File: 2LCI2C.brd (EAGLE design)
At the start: 40 x 20 mm, 38 parts, among them IC1 HX711-SOP16L, IC2 HX711-SOP16L, IC3 ATTINY84-SOIC14, J1 ICSP-PIN, J3 Load Cell, J4 Load Cell, Q1 2N3906, Q2 2N3906

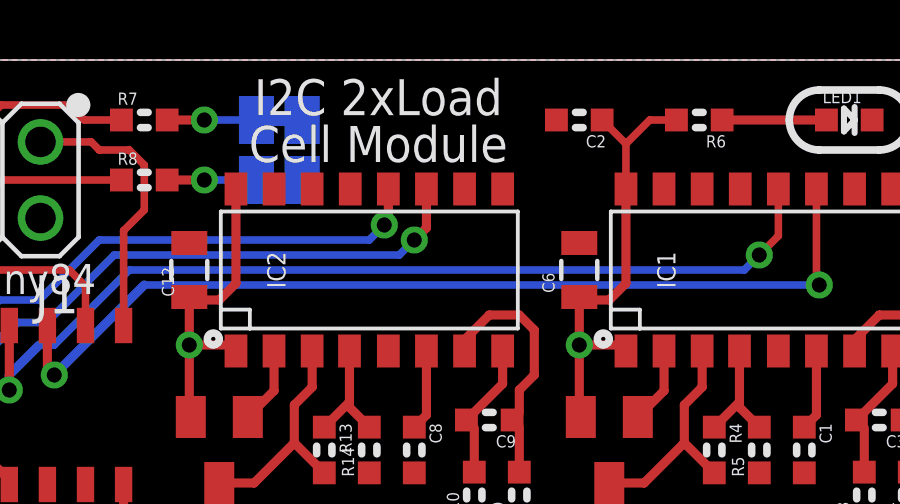
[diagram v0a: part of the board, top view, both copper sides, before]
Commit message: Changed sample rate from 10Hz to 80Hz
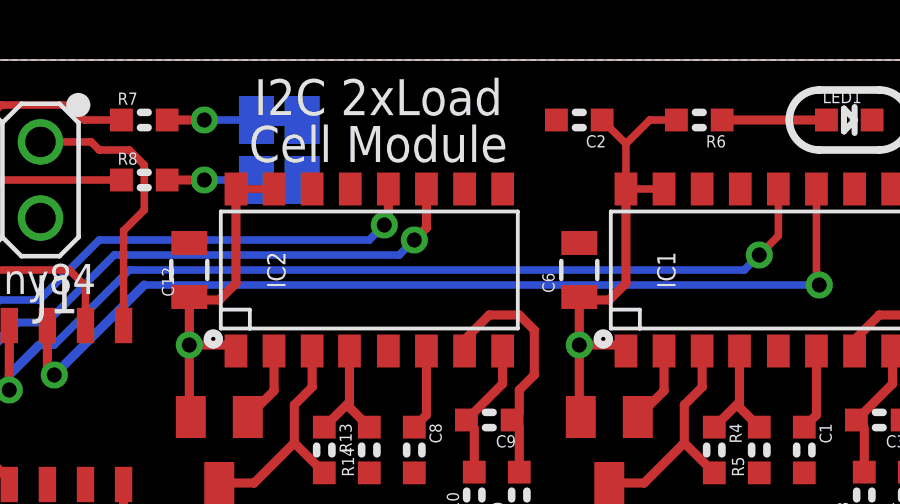
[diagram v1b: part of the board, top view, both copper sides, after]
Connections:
- net GND: no longer IC1.15, IC2.15
- net VCC: now also IC1.15, IC2.15
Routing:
- net VCC: track 34.5 -> 37.0 mm
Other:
- board text added: "v1.0"
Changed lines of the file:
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@@
 </layers>
 <board>
-<fusionsync huburn="a.cGVyc29uYWw6dWUyZDliZmNi" projecturn="a.cGVyc29uYWw6dWUyZDliZmNiIzIwMjAwNjA1MzA0OTA2NTgx" f3durn="urn:adsk.wipprod:dm.lineage:xVkUg9DcS7uGuJ_e9RHQ6Q" pcbguid="" lastpulledtime="" lastsyncedchangeguid="658b777b-6f72-af3e-08d3-df1b217e5c50" latestrevisionid="7995fdce-4818-4739-b131-21203edd6466" lastsyncedrevisionid="7995fdce-4818-4739-b131-21203edd6466" lastboardhashguid="d6e5dbb6-b330-d021-be14-3f51137d8661" lastpushedtime="2020-06-30T10:32:49Z" linktopcb3d="true"/>
+<fusionsync huburn="a.cGVyc29uYWw6dWUyZDliZmNi" projecturn="a.cGVyc29uYWw6dWUyZDliZmNiIzIwMjAwNjA1MzA0OTA2NTgx" f3durn="urn:adsk.wipprod:dm.lineage:xVkUg9DcS7uGuJ_e9RHQ6Q" pcbguid="" lastpulledtime="" lastsyncedchangeguid="658b777b-6f72-af3e-08d3-df1b217e5c50" latestrevisionid="7995fdce-4818-4739-b131-21203edd6466" lastsyncedrevisionid="7995fdce-4818-4739-b131-21203edd6466" lastboardhashguid="d6e5dbb6-b330-d021-be14-3f51137d8661" lastpushedtime="2020-06-30T10:32:49Z" linktopcb3d="false"/>
 <plain>
 <wire x1="0" y1="18" x2="0" y2="2" width="0" layer="20"/>
@@
 <wire x1="19.5" y1="16" x2="19.5" y2="18" width="0.254" layer="22"/>
 <wire x1="18.5" y1="19" x2="19.5" y2="18" width="0.254" layer="22" curve="-90"/>
+<text x="10.42" y="10.3" size="1" layer="22" font="vector" ratio="18" distance="30" rot="MR0">v1.0</text>
 </plain>
 <attributes>
@@
 <contactref element="C8" pad="2"/>
 <contactref element="IC2" pad="14"/>
-<contactref element="IC2" pad="15"/>
 <contactref element="R14" pad="1"/>
 <contactref element="C10" pad="2"/>
@@
 <contactref element="C1" pad="2"/>
 <contactref element="IC1" pad="14"/>
-<contactref element="IC1" pad="15"/>
 <contactref element="C6" pad="2"/>
 <contactref element="J1" pad="6"/>
@@
 <wire x1="4.19" y1="5.85" x2="2.55" y2="5.85" width="0.3048" layer="1"/>
 <wire x1="2.55" y1="5.85" x2="2" y2="5.9" width="0.254" layer="1"/>
+<contactref element="IC1" pad="15"/>
+<contactref element="IC2" pad="15"/>
+<wire x1="16.825" y1="15.7" x2="15.555" y2="15.7" width="0.254" layer="1"/>
+<wire x1="29.825" y1="15.7" x2="28.555" y2="15.7" width="0.254" layer="1"/>
 </signal>
 <signal name="SCK_SCL">

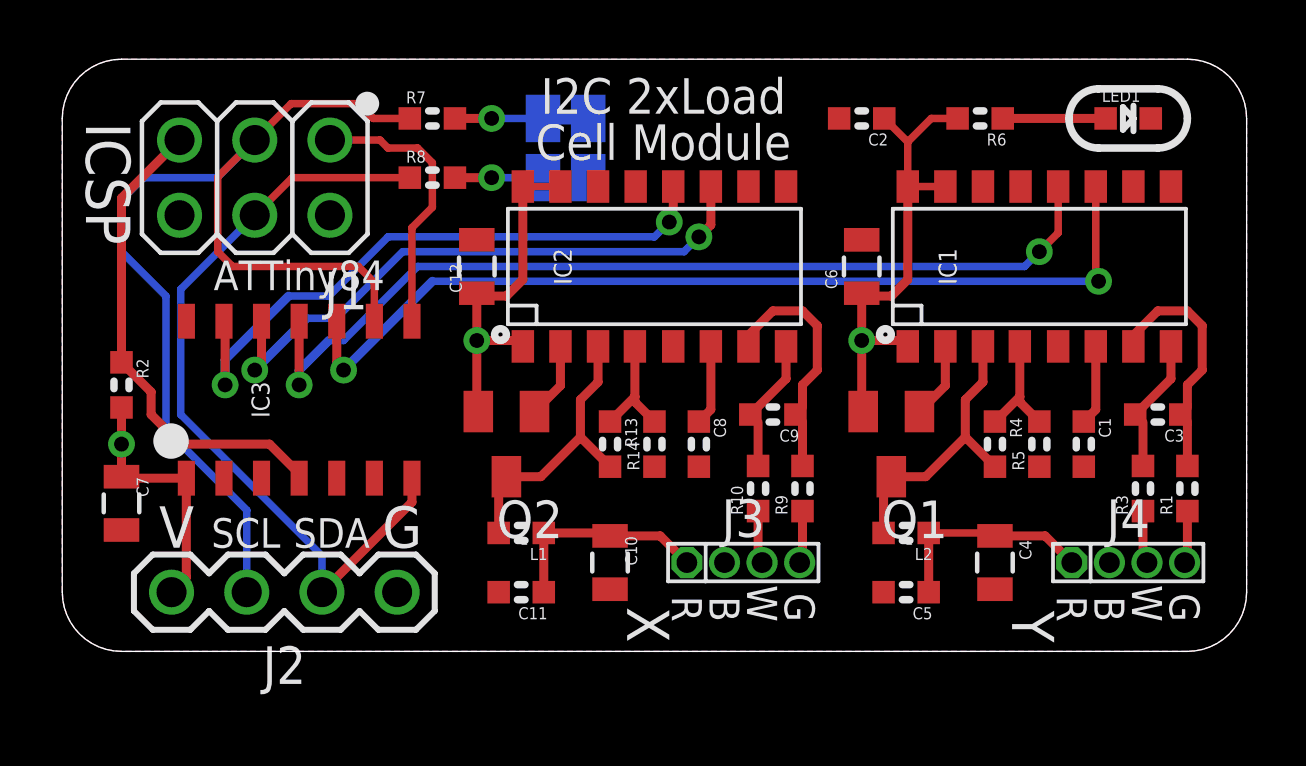
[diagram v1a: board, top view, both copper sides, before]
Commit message: Added fiducials for re-release v1.0
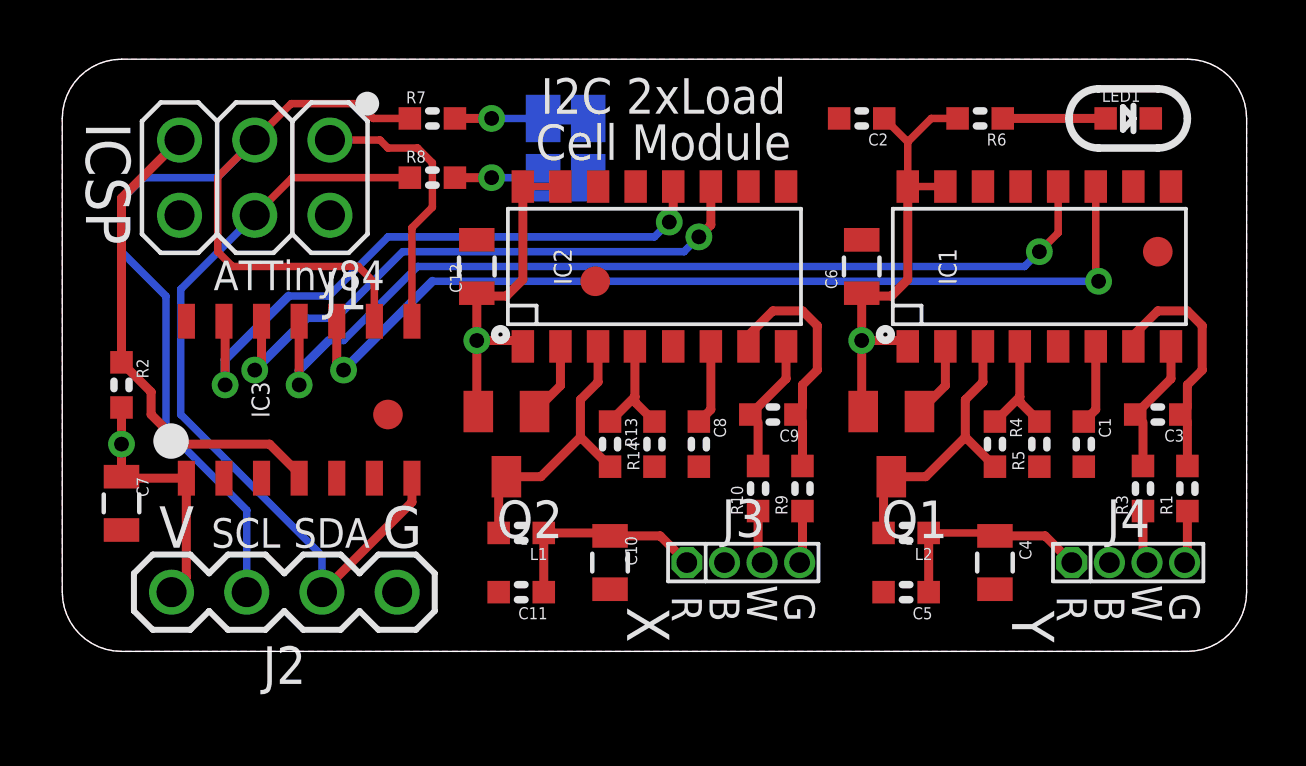
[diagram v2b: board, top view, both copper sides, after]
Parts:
- added U$10, U$11, U$5: FIDUCIAL1X2.5, SuperHouse-Symbols:FIDUCIAL-1X2.5
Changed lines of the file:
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@@
 <layer number="27" name="tValues" color="7" fill="1" visible="no" active="yes"/>
 <layer number="28" name="bValues" color="7" fill="1" visible="no" active="yes"/>
-<layer number="29" name="tStop" color="7" fill="3" visible="no" active="yes"/>
-<layer number="30" name="bStop" color="7" fill="6" visible="no" active="yes"/>
+<layer number="29" name="tStop" color="7" fill="3" visible="yes" active="yes"/>
+<layer number="30" name="bStop" color="7" fill="6" visible="yes" active="yes"/>
 <layer number="31" name="tCream" color="7" fill="4" visible="no" active="yes"/>
 <layer number="32" name="bCream" color="7" fill="5" visible="no" active="yes"/>
@@
 <layer number="37" name="tTest" color="7" fill="1" visible="no" active="yes"/>
 <layer number="38" name="bTest" color="7" fill="1" visible="no" active="yes"/>
-<layer number="39" name="tKeepout" color="4" fill="11" visible="no" active="yes"/>
-<layer number="40" name="bKeepout" color="1" fill="11" visible="no" active="yes"/>
-<layer number="41" name="tRestrict" color="4" fill="10" visible="no" active="yes"/>
-<layer number="42" name="bRestrict" color="1" fill="10" visible="no" active="yes"/>
+<layer number="39" name="tKeepout" color="4" fill="11" visible="yes" active="yes"/>
+<layer number="40" name="bKeepout" color="1" fill="11" visible="yes" active="yes"/>
+<layer number="41" name="tRestrict" color="4" fill="10" visible="yes" active="yes"/>
+<layer number="42" name="bRestrict" color="1" fill="10" visible="yes" active="yes"/>
 <layer number="43" name="vRestrict" color="2" fill="10" visible="no" active="yes"/>
 <layer number="44" name="Drills" color="7" fill="1" visible="yes" active="yes"/>
@@
 </layers>
 <board>
-<fusionsync huburn="a.cGVyc29uYWw6dWUyZDliZmNi" projecturn="a.cGVyc29uYWw6dWUyZDliZmNiIzIwMjAwNjA1MzA0OTA2NTgx" f3durn="urn:adsk.wipprod:dm.lineage:xVkUg9DcS7uGuJ_e9RHQ6Q" pcbguid="" lastpulledtime="" lastsyncedchangeguid="658b777b-6f72-af3e-08d3-df1b217e5c50" latestrevisionid="7995fdce-4818-4739-b131-21203edd6466" lastsyncedrevisionid="7995fdce-4818-4739-b131-21203edd6466" lastboardhashguid="d6e5dbb6-b330-d021-be14-3f51137d8661" lastpushedtime="2020-06-30T10:32:49Z" linktopcb3d="false"/>
+<fusionsync huburn="a.cGVyc29uYWw6dWUyZDliZmNi" projecturn="a.cGVyc29uYWw6dWUyZDliZmNiIzIwMjAwNjA1MzA0OTA2NTgx" f3durn="urn:adsk.wipprod:dm.lineage:xVkUg9DcS7uGuJ_e9RHQ6Q" pcbguid="" lastpulledtime="" lastsyncedchangeguid="658b777b-6f72-af3e-08d3-df1b217e5c50" latestrevisionid="7995fdce-4818-4739-b131-21203edd6466" lastsyncedrevisionid="7995fdce-4818-4739-b131-21203edd6466" lastboardhashguid="d6e5dbb6-b330-d021-be14-3f51137d8661" lastpushedtime="2020-06-30T10:32:49Z" linktopcb3d="true"/>
 <plain>
 <wire x1="0" y1="18" x2="0" y2="2" width="0" layer="20"/>
@@
 <attribute name="VALUE" x="17.4001" y="16" size="0.02" layer="28" rot="MR180"/>
 </element>
+<element name="U$5" library="SuperHouse-Symbols" library_urn="urn:adsk.eagle:library:13228893" package="FIDUCIAL-1X2.5" package3d_urn="urn:adsk.eagle:package:13228898/1" value="FIDUCIAL1X2.5" x="37" y="13.5" smashed="yes"/>
+<element name="U$10" library="SuperHouse-Symbols" library_urn="urn:adsk.eagle:library:13228893" package="FIDUCIAL-1X2.5" package3d_urn="urn:adsk.eagle:package:13228898/1" value="FIDUCIAL1X2.5" x="18" y="12.5" smashed="yes"/>
+<element name="U$11" library="SuperHouse-Symbols" library_urn="urn:adsk.eagle:library:13228893" package="FIDUCIAL-1X2.5" package3d_urn="urn:adsk.eagle:package:13228898/1" value="FIDUCIAL1X2.5" x="11" y="8" smashed="yes"/>
 </elements>
 <signals>
